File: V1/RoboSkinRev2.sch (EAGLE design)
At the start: 50 parts, among them U1 AK9750, U2 FDC2114RGHT, U3 ADS1015, U4 LSM6DS3DOT_INDICATION, U5 VL53L1XSMD

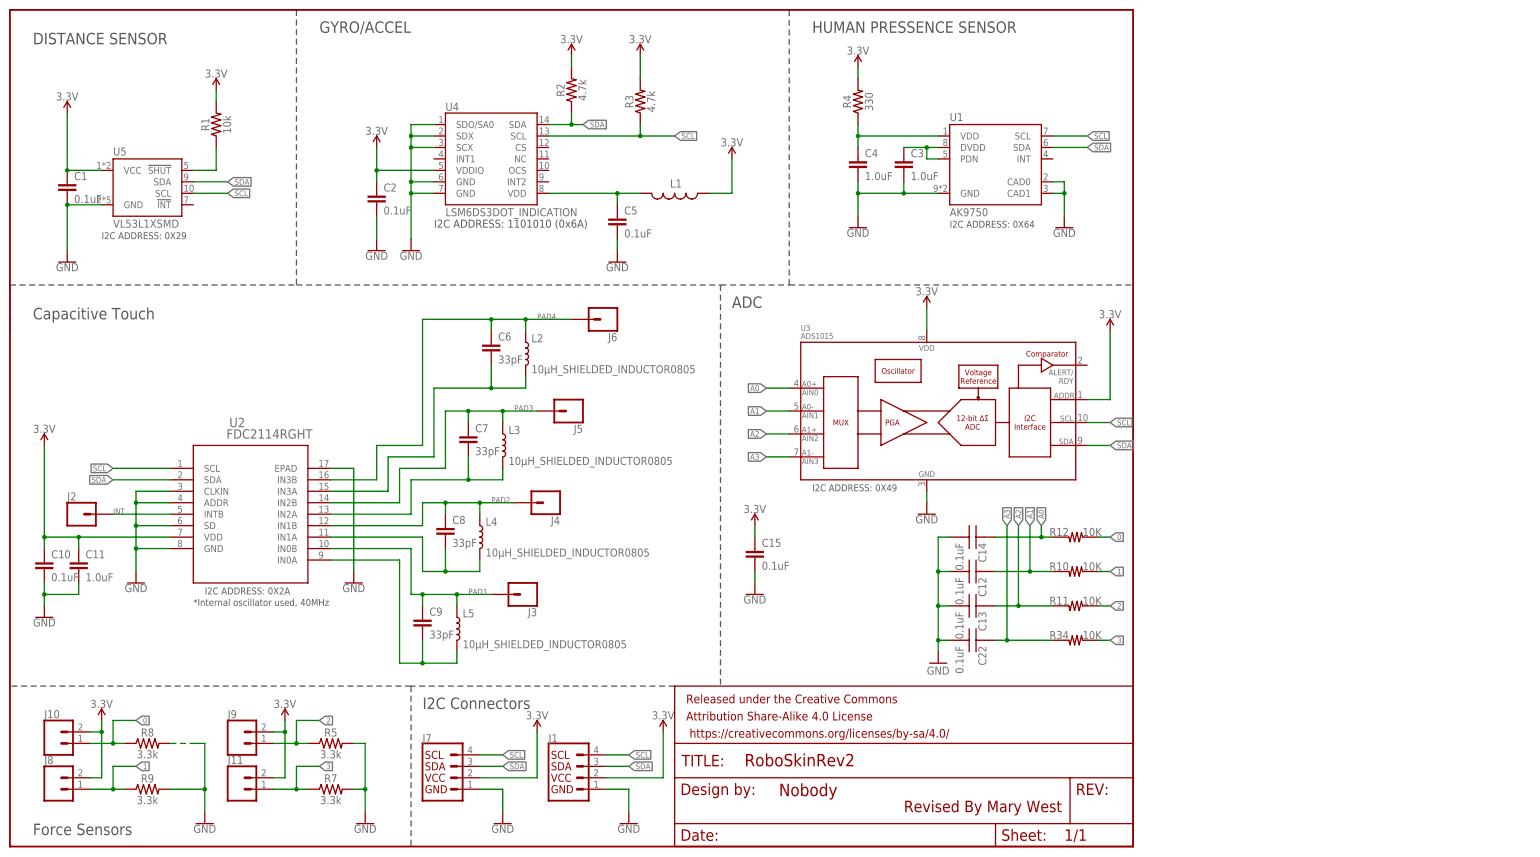
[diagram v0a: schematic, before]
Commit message: NEw PCB formfactor with added circuits, adding BOM, adding PVF
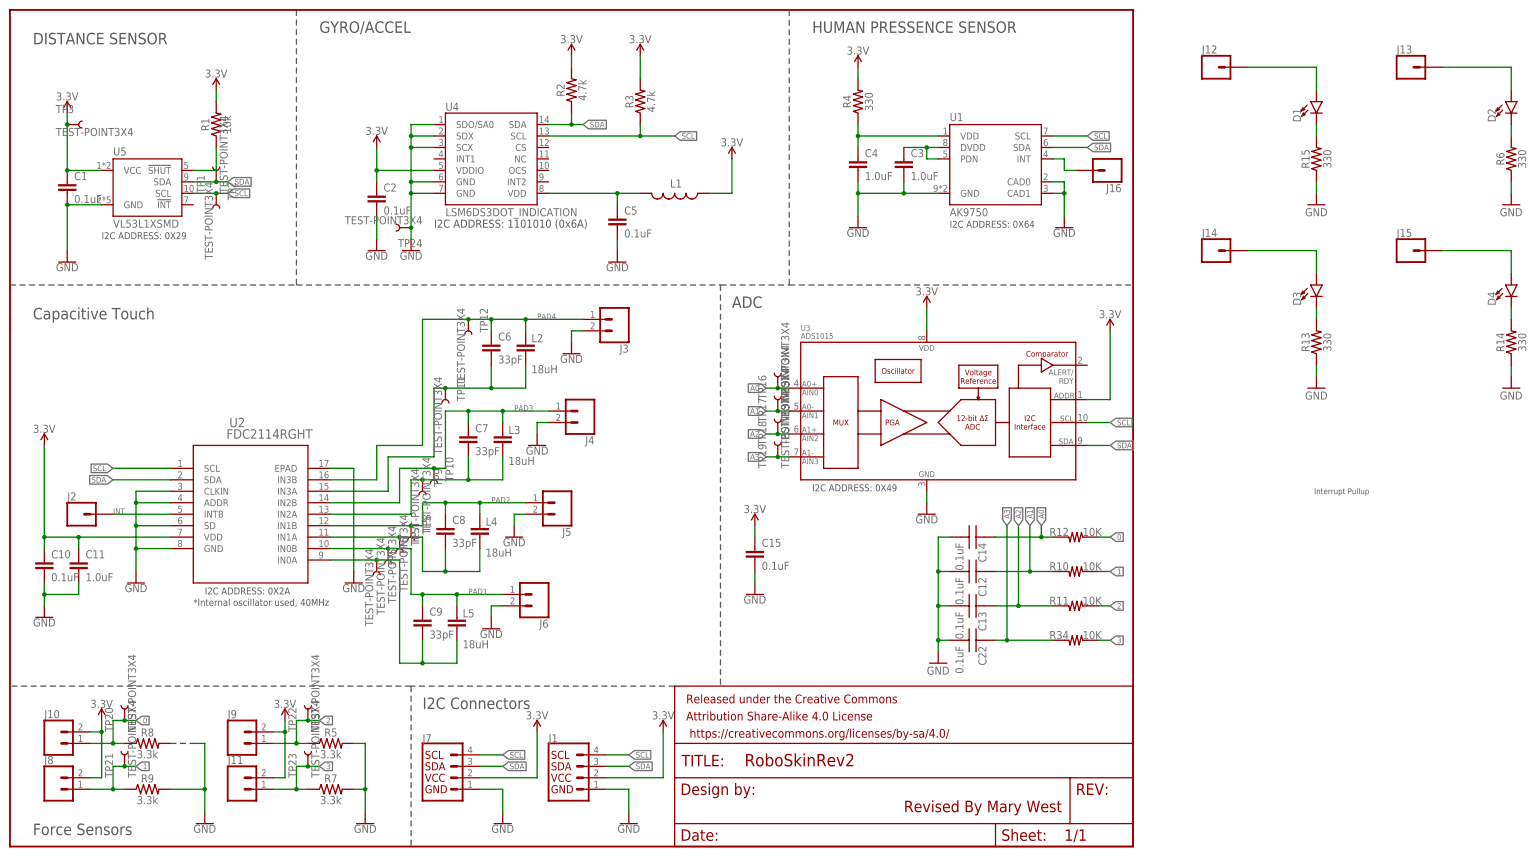
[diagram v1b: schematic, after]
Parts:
- added D1, D2, D3, D4: (no value), SparkFun-LED:LED1206
- added J12, J13, J14, J15: (no value), SparkFun-Connectors:CONN_01
- added J16: (no value), SparkFun-Connectors:CONN_01PTH_NO_SILK_YES_STOP
- added R13, R14, R15, R6: 330, SparkFun-Resistors:330OHM-0603-1/10W-1%
- added TP1, TP10, TP11, TP12, TP16, TP17, TP18, TP19, TP2, TP20, TP21, TP22, TP23, TP24, TP3, TP5, TP6, TP7, TP8, TP9: TEST-POINT3X4, SparkFun-Connectors:TEST-POINT3X4
- J3, J4, J5, J6: device SparkFun-Connectors:CONN_01 -> SparkFun-Connectors:CONN_02
- L2, L3, L4, L5: value 10μH_SHIELDED_INDUCTOR0805 -> 18uH; device SparkFun-Coils:10μH_SHIELDED_INDUCTOR0805 -> SparkFun-Retired:100UF6.3V20%(1210)
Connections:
- new net D1: D2.A, J13.1
- new net D2: D3.A, J14.1
- new net D3: D4.A, J15.1
- new net D7: D1.A, J12.1
- new net N$11: J16.1, U1.INT
- new net N$4: D1.C, R15.2
- new net N$5: D2.C, R6.2
- new net N$7: D3.C, R13.2
- new net N$9: D4.C, R14.2
- net 0: now also TP20.1
- net 1: now also TP21.1
- net 2: now also TP22.1
- net 3: now also TP23.1
- net 3.3V: now also TP3.1
- net A0: now also TP16.1
- net A1: now also TP17.1
- net A2: now also TP18.1
- net A3: now also TP19.1
- net GND: now also J3.2, J4.2, J5.2, J6.2, R13.1, R14.1, R15.1, R6.1, TP24.1
- net N$10: now also TP9.1
- net N$12: now also TP7.1
- net N$14: now also TP5.1
- net N$8: now also TP11.1
- net PAD1: now also J6.1, TP6.1; no longer J3.1
- net PAD2: now also J5.1, TP8.1; no longer J4.1
- net PAD3: now also J4.1, TP10.1; no longer J5.1
- net PAD4: now also J3.1, TP12.1; no longer J6.1
- net SCL: now also TP2.1
- net SDA: now also TP1.1
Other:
- note added: "Interrupt Pullup"
- moved on the sheet: L2, L3, L4, L5
